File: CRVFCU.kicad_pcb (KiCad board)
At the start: 4 copper layers, 50 x 100 mm, 154 parts, among them J1 TagConnect_TC2030, J2 Conn_01x02, J3 USB_C_Receptacle_USB2.0_16P, J4 Micro_SD_Card_Det2, J5 Conn_01x02, Q3 DMG2301L, Q4 BC818, Q5 DMG2301L, Q6 DMG2301L, U1 MS5611-01BA, U10 W25Q128JVS, U11 EClamp2515K, U12 ESDALC6V1W5, U13 USBLC6-2SC6, U14 USBLC6-2SC6, U15 MAX17049, U16 SI7232DN-T1, U17 SN74LV1T34DCK, U2 STM32H747IITx, U3 LIS2MDL, U4 ICM-45686, U5 FXMA108, U6 AP1117-50, U7 AP1117-33, U8 SI7232DN-T1, U9 USBLC6-4SC6, Y1 32.768khz, Y2 Crystal_GND24, Y3 32.768khz

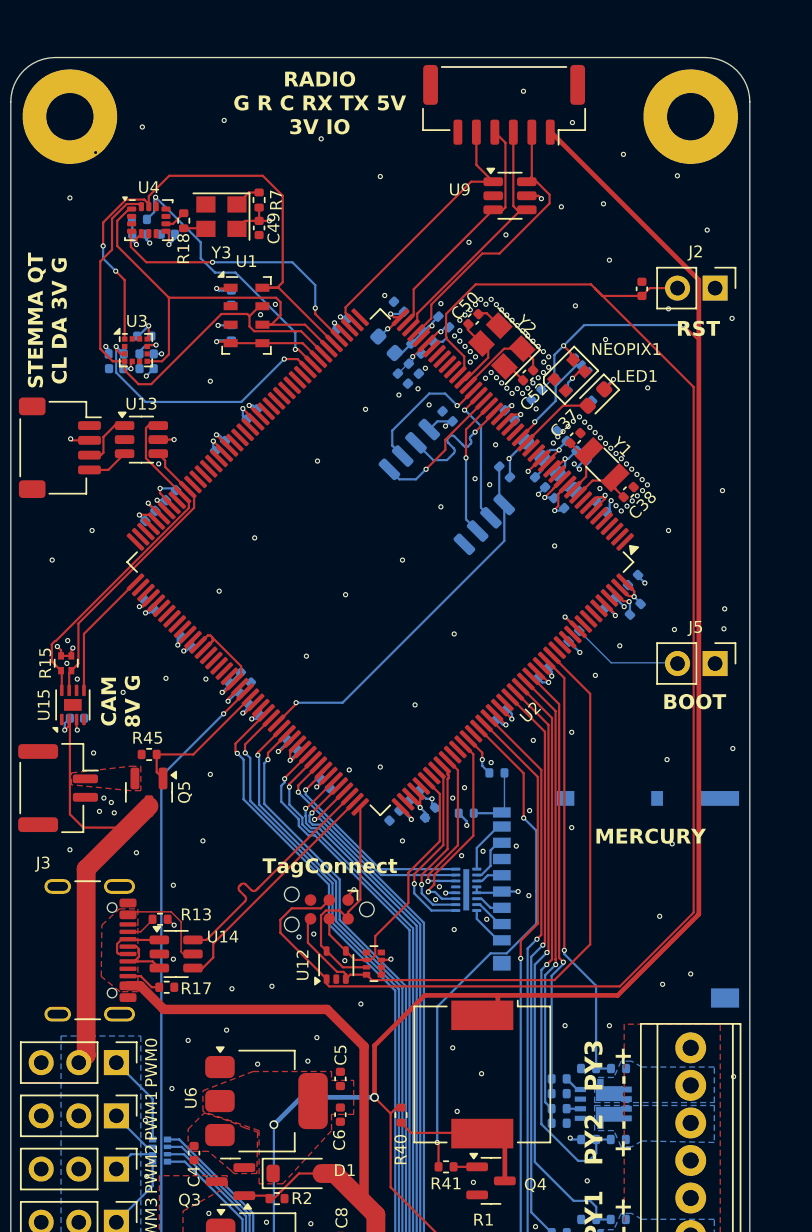
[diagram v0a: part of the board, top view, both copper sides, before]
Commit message: added silkscreens
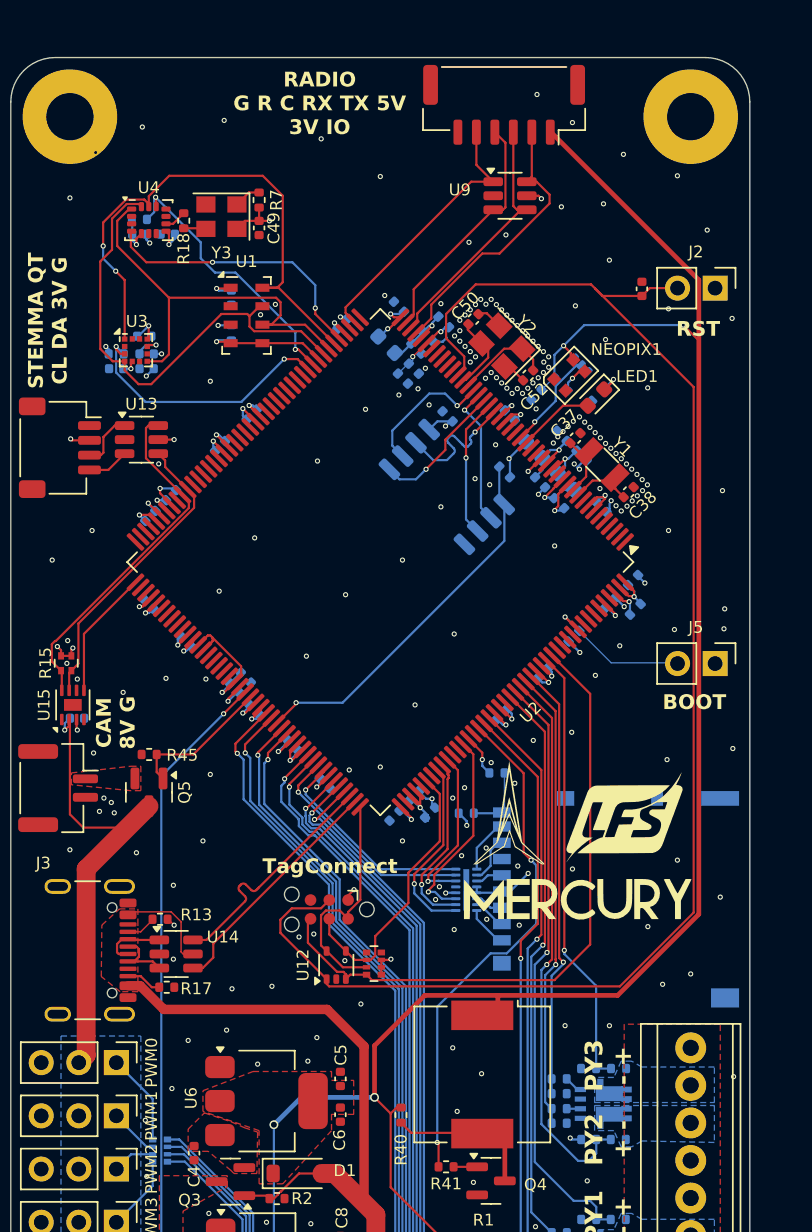
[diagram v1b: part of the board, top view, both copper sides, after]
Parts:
- added G***: LOGO, LOGO, F.Cu at (80.4, 77.0)
- added G***: LOGO, LOGO, F.Cu at (81.4, 71.5)
- added G***: LOGO, LOGO, F.Cu at (73.7, 71.5)
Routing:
- net +3V3: track 88.3 -> 89.5 mm
- net GND: vias 234 -> 235
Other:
- board text added: "Mercury STM32H747 FCU V1.0 2025 Designed By Kaiwen Zheng - Leviathan Flight Systems Designed For Hayden S Cervienic - CRV Components"
- board text removed: "MERCURY"
- board text removed: "Mercury H747 FCU V1.0 2025 Kaiwen Zheng"

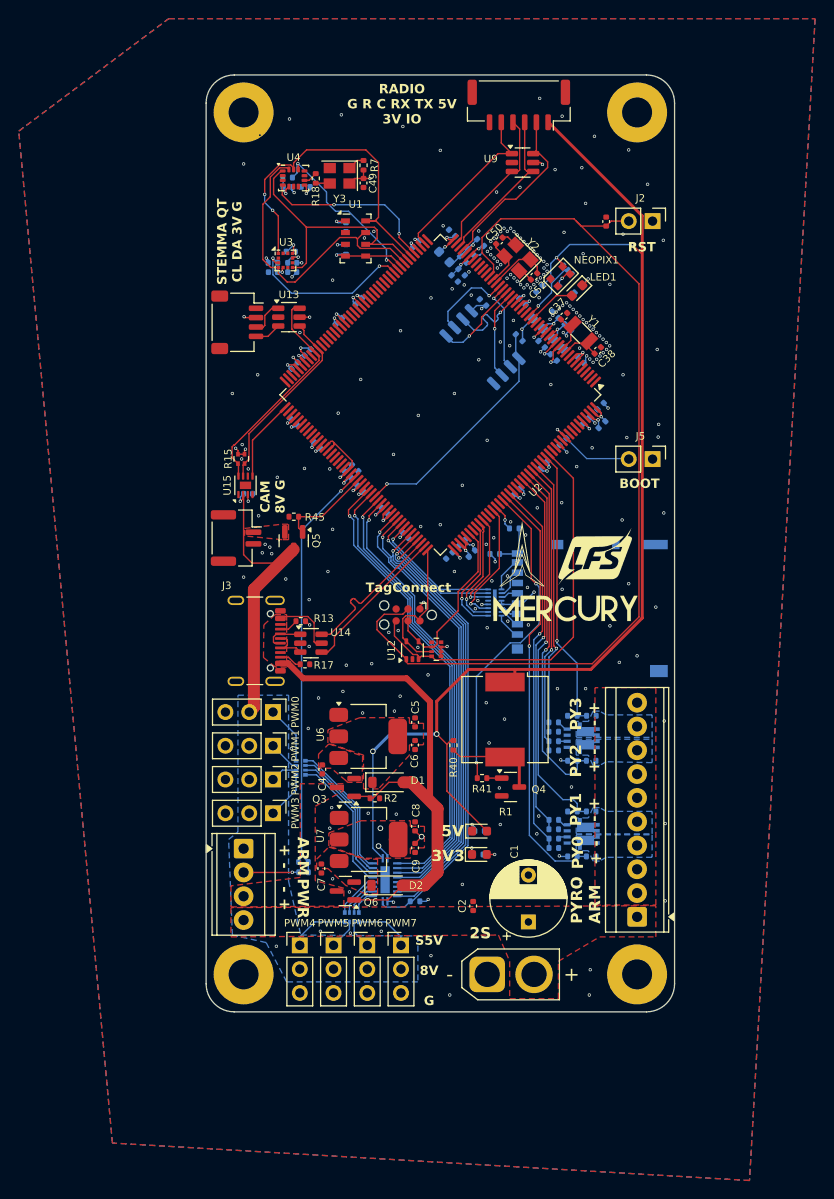
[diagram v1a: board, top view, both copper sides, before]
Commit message: tuned silkscreens
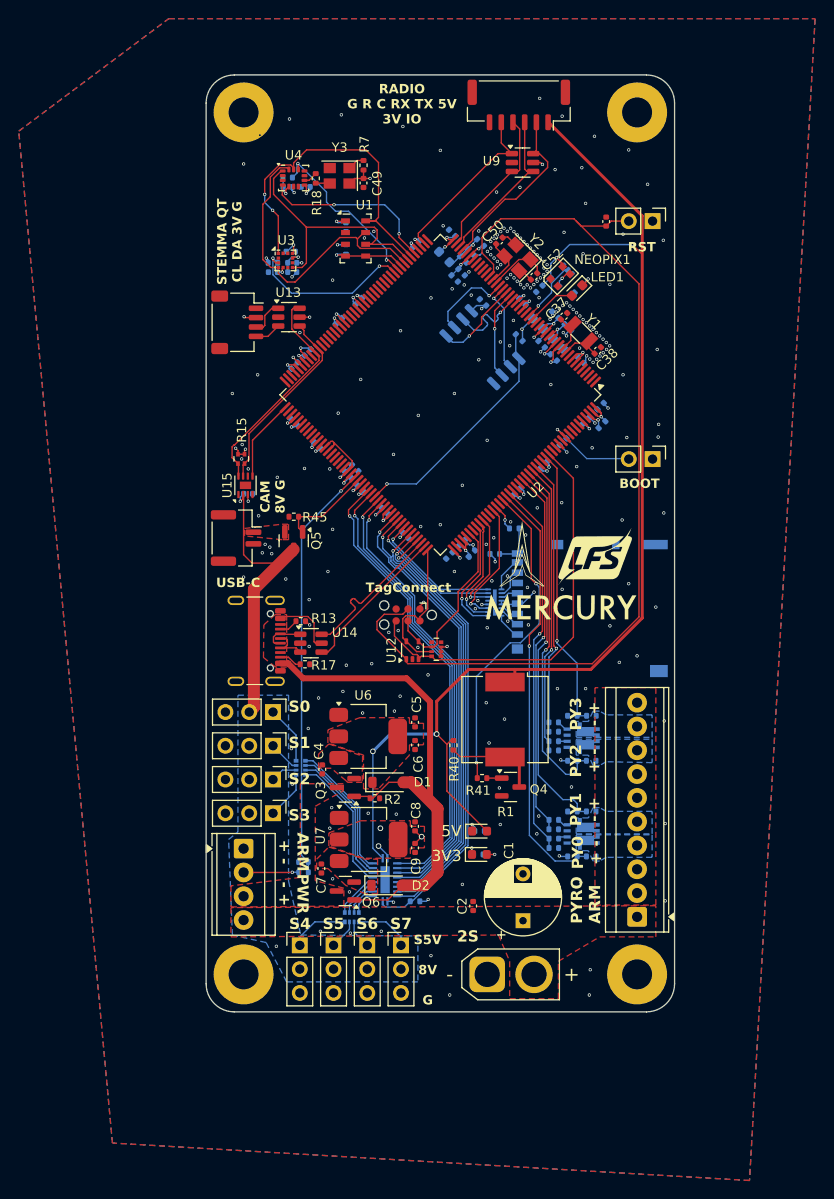
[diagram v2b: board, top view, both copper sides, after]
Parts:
- moved G*** 2.60 mm to (77.8, 76.9)
- moved C1 0.59 mm to (73.8, 110.3)
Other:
- board text added: "MicroSD"
- board text added: "S0 S1 S2 S3"
- board text added: "S4"
- board text added: "S5"
- board text added: "S6"
- board text added: "S7"
- board text added: "USB-C"

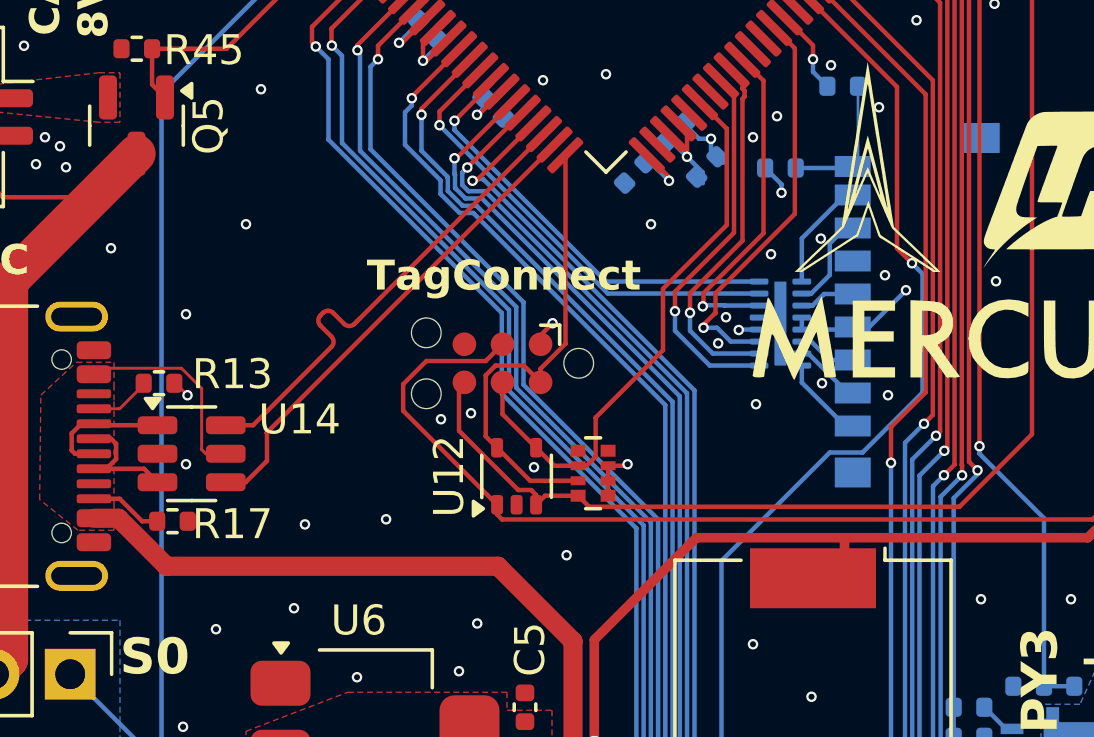
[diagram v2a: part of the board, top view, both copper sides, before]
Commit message: fixed drc silkscreens
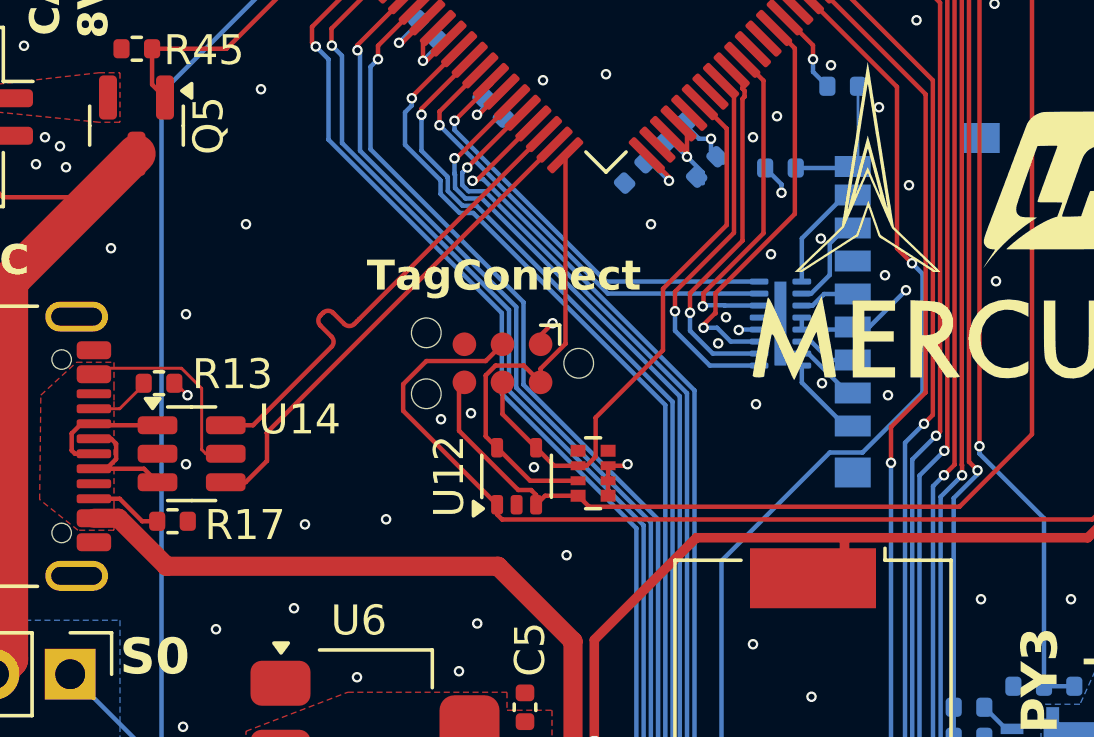
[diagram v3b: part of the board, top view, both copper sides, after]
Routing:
- net GND: vias 235 -> 236
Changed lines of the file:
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@@
 		(tags "resistor")
 		(property "Reference" "R17"
-			(at -2 -0.1 0)
+			(at -2.42 -0.13 0)
 			(layer "F.SilkS")
 			(effects
@@
 		(tags "capacitor")
 		(property "Reference" "C24"
-			(at 0.333172 1.308147 45)
+			(at 0.502878 1.26572 45)
 			(layer "B.SilkS")
 			(effects
@@
 		(tags "capacitor")
 		(property "Reference" "C23"
-			(at 0 1.16 45)
+			(at -0.529498 1.237436 45)
 			(layer "B.SilkS")
 			(effects
@@
 		(size 0.35)
 		(drill 0.2)
+		(layers "F.Cu" "B.Cu")
+		(free yes)
+		(net 2)
+	)
+	(via
+		(at 75.1 71.7)
+		(size 0.35)
+		(drill 0.2)

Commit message: some more silkscreen changes
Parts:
- removed the G*** at (81.4, 71.5)
- removed the G*** at (73.7, 71.5)
- added G***: LOGO, LOGO, F.Cu at (77.8, 71.8)
- added G***: LOGO, LOGO, B.Cu at (51.3, 26.3)
- moved G*** 1.40 mm to (77.8, 78.3)
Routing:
- net +3V3: track 89.5 -> 88.1 mm

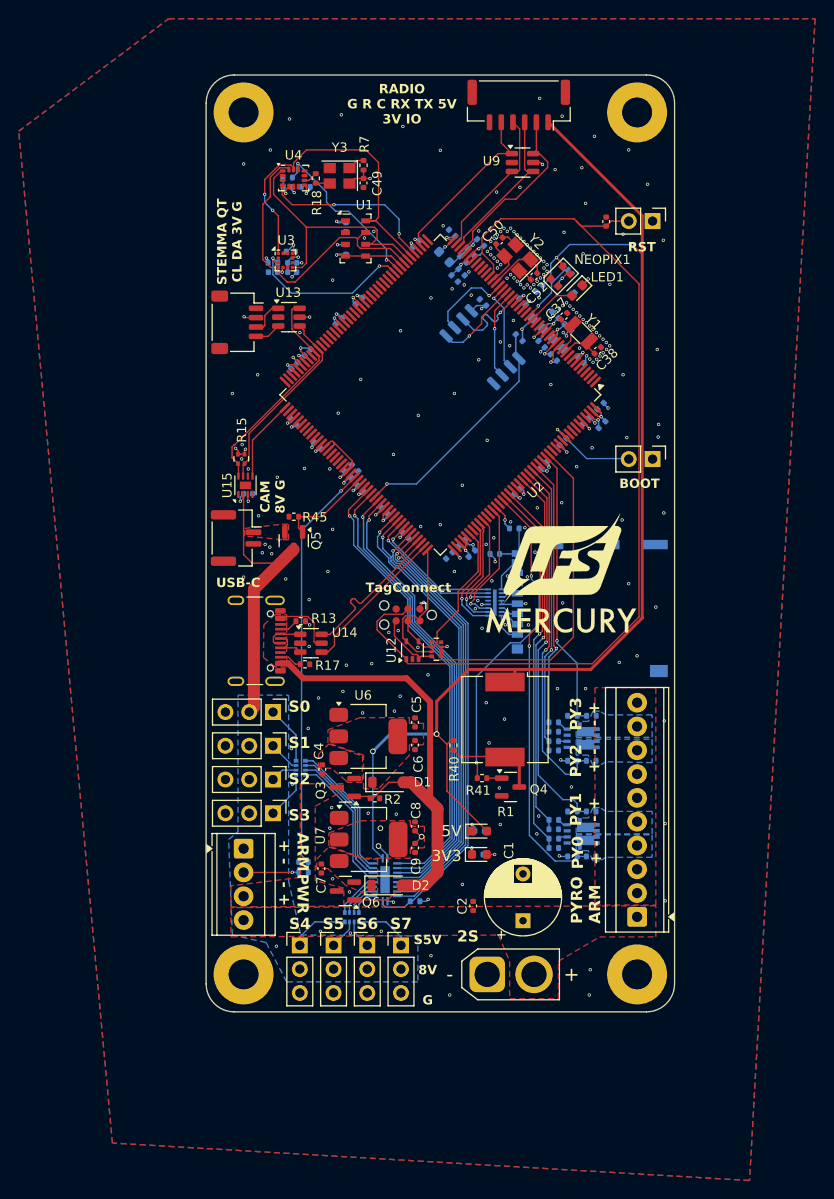
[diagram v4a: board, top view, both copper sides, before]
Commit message: changed silkscreens and via locations for aesthetics
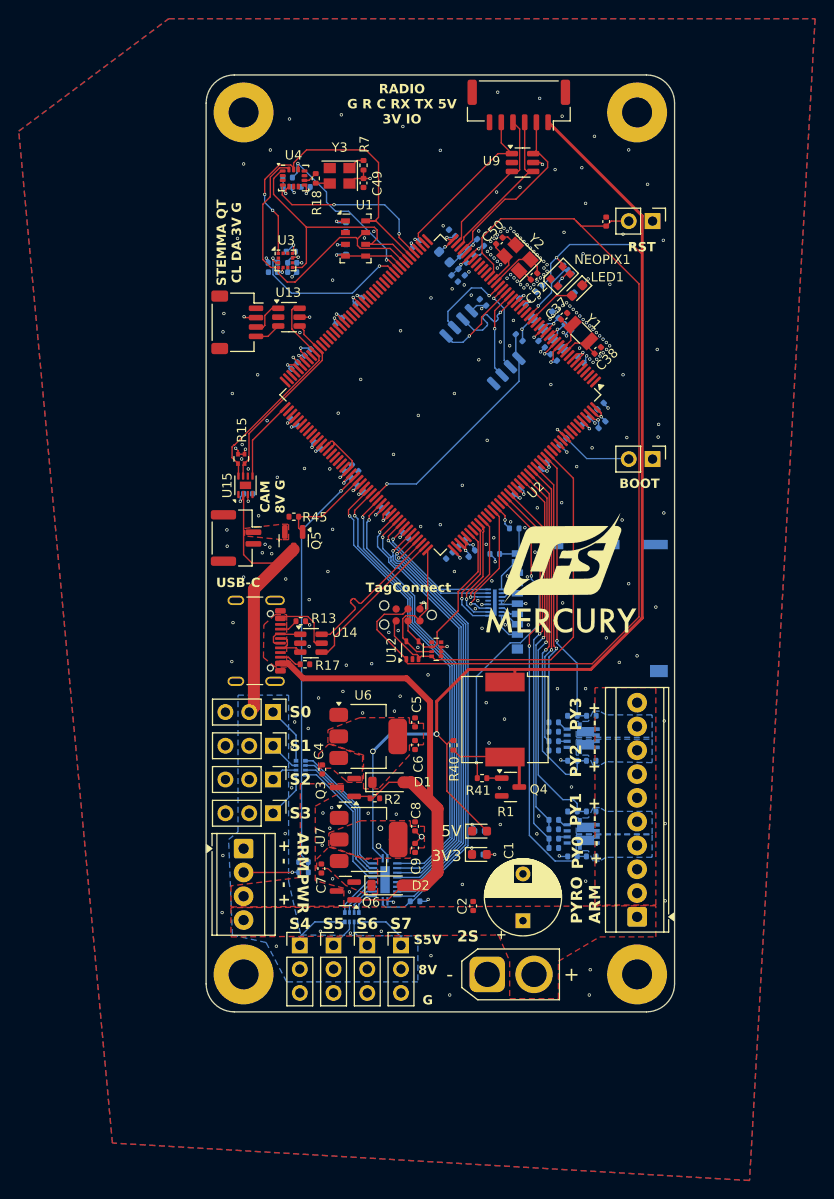
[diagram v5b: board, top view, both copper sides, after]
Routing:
- net GND: vias 236 -> 250
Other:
- board text added: "S0"
- board text added: "S1"
- board text added: "S2"
- board text added: "S3"
- board text removed: "S0 S1 S2 S3"
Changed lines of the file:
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@@
 		(tags "Through hole pin header THT 1x03 2.54mm single row")
 		(property "Reference" "PWM1"
-			(at -0.16 -3.61 180)
+			(at -0.16 -3.61 0)
 			(layer "F.SilkS")
 			(hide yes)
@@
 	)
 	(gr_text "STEMMA QT\nCL DA 3V G"
-		(at 43.9 37.8 90)
+		(at 43.843682 37.901615 90)
 		(layer "F.SilkS")
 		(effects
@@
 		)
 	)
+	(gr_text "S1"
+		(at 50.06 91.6 0)
+		(layer "F.SilkS")
+		(effects
+			(font
+				(size 1.2 1.2)
+				(thickness 0.2)
+				(bold yes)
+			)
+		)
+	)
 	(gr_text "PWR\n- +"
 		(at 47.67 107.4 270)
@@
 		)
 	)
+	(gr_text "S3"
+		(at 50.06 98.8 0)
+		(layer "F.SilkS")
+		(effects
+			(font
+				(size 1.2 1.2)
+				(thickness 0.2)
+				(bold yes)
+			)
+		)
+	)
 	(gr_text "S5V\n\n8V\n\nG"
 		(at 63.65 119.33 0)
@@
 		)
 	)
+	(gr_text "S2"
+		(at 50.06 95.2 0)
+		(layer "F.SilkS")
+		(effects
+			(font
+				(size 1.2 1.2)
+				(thickness 0.2)
+				(bold yes)
+			)
+		)
+	)
 	(gr_text "RADIO\nG R C RX TX 5V\n3V IO"
 		(at 60.9 25.3 0)
@@
 		)
 	)
-	(gr_text "S0\n\nS1\n\nS2\n\nS3"
-		(at 49.96 99.71 0)
+	(gr_text "S0"
+		(at 50.06 88 0)
 		(layer "F.SilkS")
 		(effects
@@
 				(bold yes)
 			)
-			(justify bottom)
 		)
 	)
@@
 	)
 	(via
+		(at 42.74 82.61)
+		(size 0.35)
+		(drill 0.2)
+		(layers "F.Cu" "B.Cu")
+		(free yes)
+		(net 2)
+	)
+	(via
 		(at 76.036447 41.31066)
 		(size 0.35)
@@
 	)
 	(via
+		(at 41.79 103.31)
+		(size 0.35)
+		(drill 0.2)
+		(layers "F.Cu" "B.Cu")
+		(free yes)
+		(net 2)
+	)
+	(via
 		(at 78.474466 47.848679)
 		(size 0.35)
@@
 	)
 	(via
-		(at 49.1 91.9)
+		(at 49.18 91.74)
 		(size 0.35)
 		(drill 0.2)
@@
 	)
 	(via
+		(at 49.45 89.06)
+		(size 0.35)
+		(drill 0.2)
+		(layers "F.Cu" "B.Cu")
+		(free yes)
+		(net 2)
+	)
+	(via
 		(at 74.27 42.4)
 		(size 0.35)
@@
 	)
 	(via
+		(at 42.25 70.3)
+		(size 0.35)
+		(drill 0.2)
+		(layers "F.Cu" "B.Cu")
+		(free yes)
+		(net 2)
+	)
+	(via
 		(at 67.55 42.41)
 		(size 0.35)
@@
 	)
 	(via
+		(at 41.8 47.42)
+		(size 0.35)
+		(drill 0.2)
+		(layers "F.Cu" "B.Cu")
+		(free yes)
+		(net 2)
+	)
+	(via
 		(at 73.915126 37.775126)
 		(size 0.35)
@@
 	)
 	(via
+		(at 52.470578 98.775887)
+		(size 0.35)
+		(drill 0.2)
+		(layers "F.Cu" "B.Cu")
+		(free yes)
+		(net 2)
+	)
+	(via
 		(at 65 28.05)
 		(size 0.35)
@@
 	)
 	(via
-		(at 43.466318 37.828385)
+		(at 43.35 37.45)
 		(size 0.35)
 		(drill 0.2)
@@
 	)
 	(via
+		(at 41.71 109.4)
+		(size 0.35)
+		(drill 0.2)
+		(layers "F.Cu" "B.Cu")
+		(free yes)
+		(net 2)
+	)
+	(via
 		(at 48.5 73.8)
 		(size 0.35)
@@
 	)
 	(via
+		(at 48.44 100.97)
+		(size 0.35)
+		(drill 0.2)
+		(layers "F.Cu" "B.Cu")
+		(free yes)
+		(net 2)
+	)
+	(via
 		(at 50.008577 47.491423)
 		(size 0.35)
@@
 	)
 	(via
+		(at 42.869128 78.452055)
+		(size 0.35)
+		(drill 0.2)
+		(layers "F.Cu" "B.Cu")
+		(free yes)
+		(net 2)
+	)
+	(via
 		(at 81.656443 47.495123)
 		(size 0.35)
@@
 	)
 	(via
-		(at 83.1 78.8)
+		(at 82.72 80.08)
 		(size 0.35)
 		(drill 0.2)
@@
 	)
 	(via
+		(at 52.39 102.21)
+		(size 0.35)
+		(drill 0.2)
+		(layers "F.Cu" "B.Cu")
+		(free yes)
+		(net 2)
+	)
+	(via
 		(at 72.500913 36.360914)
 		(size 0.35)
@@
 	)
 	(via
+		(at 46.51 56.9)
+		(size 0.35)
+		(drill 0.2)
+		(layers "F.Cu" "B.Cu")
+		(free yes)
+		(net 2)
+	)
+	(via
 		(at 81.69 50.35)
 		(size 0.35)
@@
 	)
 	(via
+		(at 41.9 45.46)
+		(size 0.35)
+		(drill 0.2)
+		(layers "F.Cu" "B.Cu")
+		(free yes)
+		(net 2)
+	)
+	(via
 		(at 71.0867 39.896445)
 		(size 0.35)
@@
 	)
 	(via
-		(at 49.2 95.7)
+		(at 49.13 96.08)
 		(size 0.35)
 		(drill 0.2)
@@
 	)
 	(via
-		(at 80 106.2)
+		(at 80.51 106.05)
 		(size 0.35)
 		(drill 0.2)
@@
 	)
 	(via
+		(at 71.12 21.84)
+		(size 0.35)
+		(drill 0.2)
+		(layers "F.Cu" "B.Cu")
+		(free yes)
+		(net 2)
+	)
+	(via
 		(at 77.5 85.5)
 		(size 0.35)
@@
 		(size 0.35)
 		(drill 0.2)
+		(layers "F.Cu" "B.Cu")
+		(free yes)
+		(net 2)
+	)
+	(via
+		(at 42.22 68.56)
+		(size 0.35)
+		(drill 0.2)
